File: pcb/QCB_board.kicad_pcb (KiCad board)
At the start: 4 copper layers, 101.6 x 128.7 mm, 216 parts, among them IC1 IP175G, J1 Conn_01x03_Socket, J10 DIN41612_02x32_AC, J2 Conn_01x04_Socket, J3 100616-2, J4 Conn_01x04, J5 Conn_01x02, J6 39-29-3086, J7 DIN41612_02x32_AC, J8 DIN41612_02x32_AC, J9 DIN41612_02x32_AC, T1 H1102NL, U1 FE1.1s, U10 M24C02-WMN, U11 USBLC6-2SC6, U12 M24C02-WMN, U13 USBLC6-2SC6, U14 USBLC6-2SC6, U2 24LC02, U3 24LC02, U4 USBLC6-2SC6, U5 USBLC6-2SC6, U6 M24C02-WMN, U7 USBLC6-2SC6, U8 M24C02-WMN, U9 USBLC6-2SC6, Y1 ABM8G-12.000MHZ-18, Y2 3225-25M-SR

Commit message: Unify passive values/footprints, add via-in-pad DRC rule, regen outputs
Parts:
- C37, C38: value 6,8n -> 6.8n
- R1: value 0R/47k -> 0R
- R11, R12, R13, R14, R15, R16, R41, R42: value 49R9 -> 49.9
- R17, R18, R19, R20, R28, R29, R31, R32, R37, R38, R39, R40, R47, R48, R49, R50, R51, R52, R53, R54: value 2R2 -> 2.2
- R33: value 6k19 -> 6.19k
- R43: value 10R -> 10
- R45, R46: value 82R -> 82
- R55, R56: value 75R -> 75
- R57, R58: value 150R -> 150
- R9: value 2k7 -> 2.7k
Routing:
- net GND: vias 3263 -> 3245

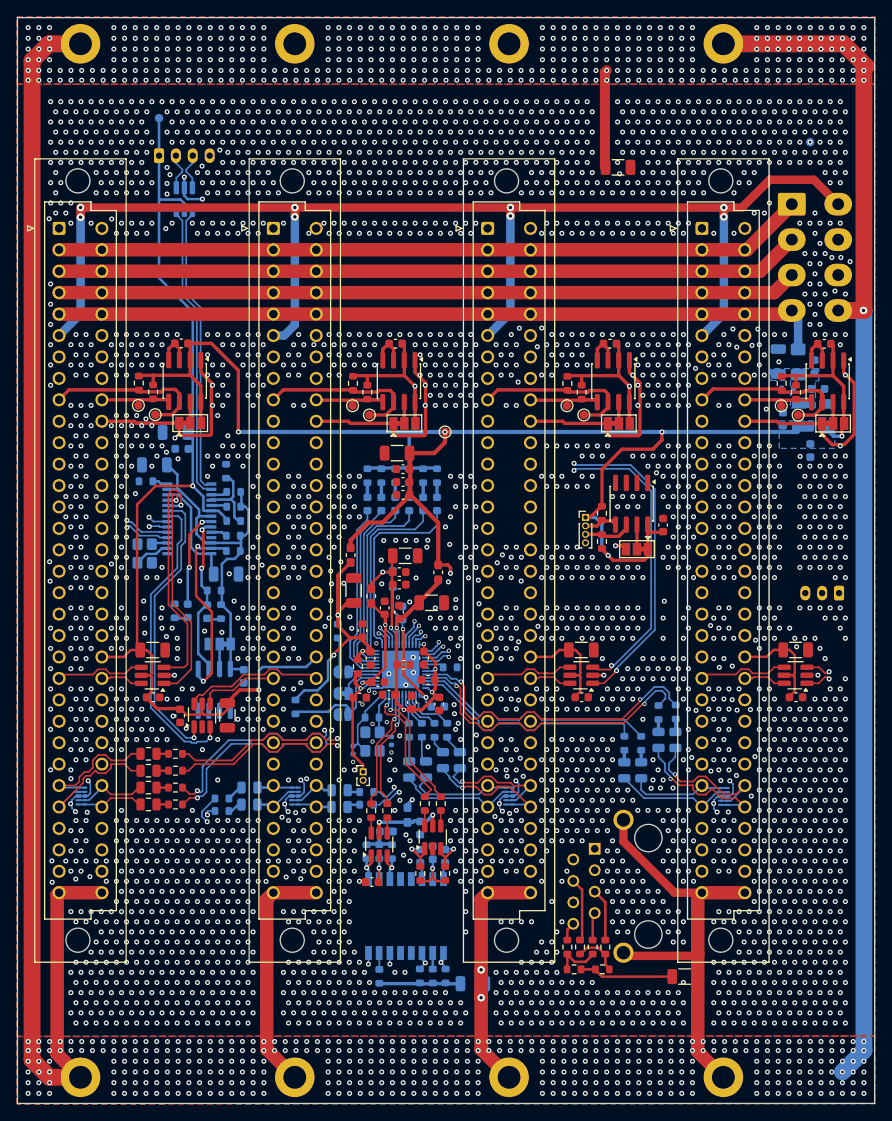
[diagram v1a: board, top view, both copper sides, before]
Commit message: Apply review checklist fixes, add fiducials, regenerate production outputs
- C41/C42 (Y2 load caps) now included in BOM
- Add USB hub crystal load caps C50/C51 (DNP), rework Y1 area placement
- 2 fiducials per side (hand assembly)
- Add IP175G, FE1.1s and UT8413A datasheets to doc/datasheet
- README: status updated (ready for prototype order), production links
- .gitignore: drop leftover SCA_board ibom.config.ini entry
- Regenerate BOM, PDFs, gerber zip, interactive BOM and 3D renders
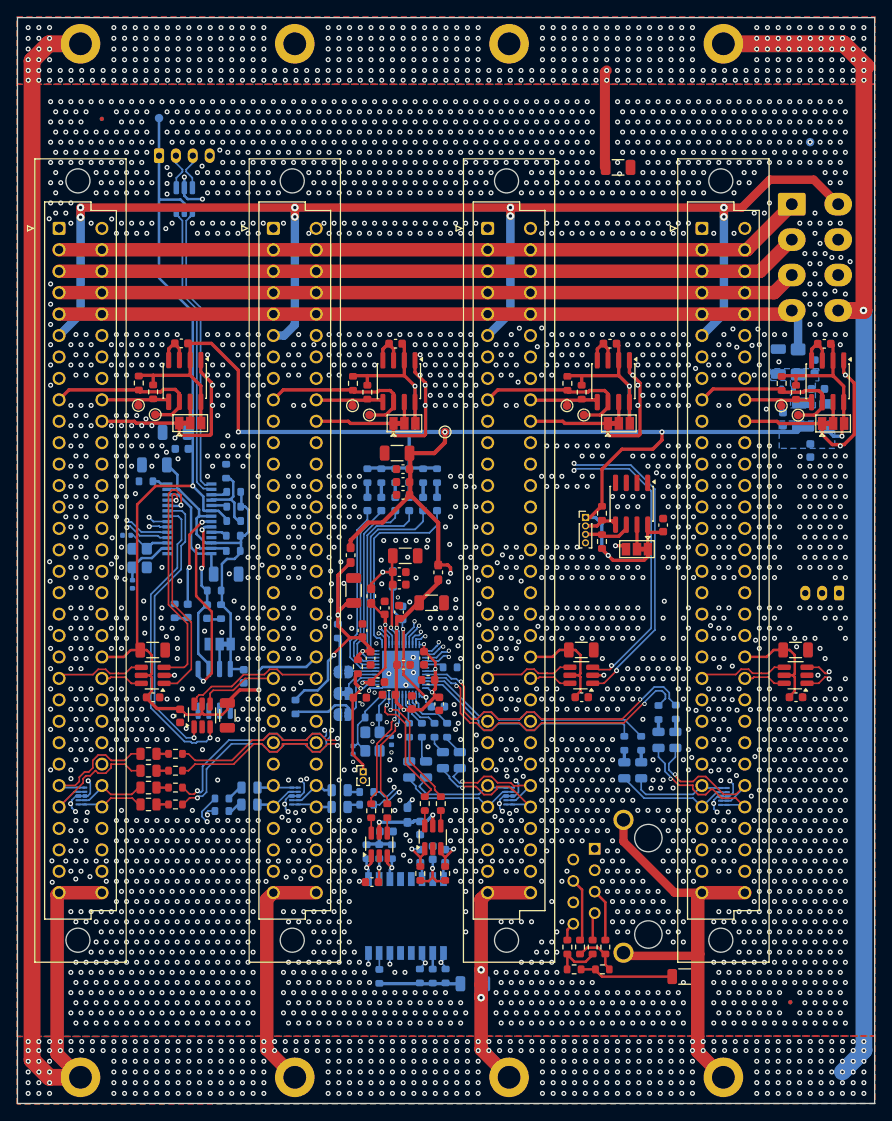
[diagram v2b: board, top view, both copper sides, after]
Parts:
- added C50: 18p, Capacitor_SMD:C_0402_1005Metric, B.Cu at (83.6, 86.1)
- added C51: 18p, Capacitor_SMD:C_0402_1005Metric, B.Cu at (84.3, 91.9)
- added FID1: Fiducial, Fiducial:Fiducial_0.5mm_Mask1mm, F.Cu at (80.7, 36.7)
- added FID2: Fiducial, Fiducial:Fiducial_0.5mm_Mask1mm, F.Cu at (162.3, 141.4)
- added FID3: Fiducial, Fiducial:Fiducial_0.5mm_Mask1mm, B.Cu at (80.7, 36.7)
- added FID4: Fiducial, Fiducial:Fiducial_0.5mm_Mask1mm, B.Cu at (162.3, 141.4)
- moved Y1 0.81 mm to (85.2, 88.8)
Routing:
- net Net-(U1-XIN): track 1.91 -> 5.32 mm
- net Net-(U1-XOUT): track 4.26 -> 6.61 mm
- net GND: vias 3245 -> 3232
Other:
- board text added: "ETH 10/100M"
- board text added: "RS485"
- board text added: "USB"
